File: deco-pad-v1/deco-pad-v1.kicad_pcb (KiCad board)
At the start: 2 copper layers, 86 parts, among them J1 AVR-ISP-6, SW1 EC11, SW2 EC11, SW3 EC11, SW4 SW_Push, U1 ATmega32U4-MU, U2 PRTR5VOU2X, Y1 16MHz

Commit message: [NZ] Still staging
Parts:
- moved H5 48.1 mm to (139.0, 148.0)
- moved J1 41.1 mm to (128.0, 89.5)
- moved SW4 40.5 mm to (118.4, 76.0), turned to 180 degrees
- moved R17 35.3 mm to (124.8, 79.2)
- moved C9 26.6 mm to (114.3, 115.1)
- moved C8 26.4 mm to (129.1, 108.8)
- moved Y1 25.7 mm to (129.1, 112.0)
- moved U1 25.6 mm to (119.7, 111.3)
- moved C10 25.3 mm to (123.1, 116.7)
- moved C7 24.9 mm to (129.1, 115.2)
- moved C14 24.6 mm to (119.9, 103.5)
- moved C15 24.6 mm to (121.9, 103.5)
- moved C12 24.5 mm to (113.5, 107.1)
- moved C13 24.5 mm to (113.5, 109.1)
- moved C11 24.2 mm to (125.3, 108.3), turned to 90 degrees
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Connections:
- SW1 pad A: E0_PAD_B -> E0_PAD_A
- SW1 pad B: E0_PAD_A -> E0_PAD_B
- SW2 pad A: E1_PAD_B -> E1_PAD_A
- SW2 pad B: E1_PAD_A -> E1_PAD_B
- SW3 pad A: E2_PAD_B -> E2_PAD_A
- SW3 pad B: E2_PAD_A -> E2_PAD_B
- U2 pad 4: VBUS -> Net-(U2-Pad4)
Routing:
- net ROW3: track 0.00 -> 73.0 mm
- net ROW2: track 0.00 -> 73.0 mm
- net ROW1: track 0.00 -> 73.0 mm
- net ROW0: track 0.00 -> 73.0 mm
- net RESET: track 0.00 -> 51.0 mm, vias 0 -> 3
- net D+: track 0.00 -> 44.4 mm
- net D-: track 0.00 -> 44.3 mm
- net GND: track 11.4 -> 39.2 mm
- net SCK: track 0.00 -> 24.4 mm
- net MISO: track 0.00 -> 22.7 mm
- net +5V: track 2.31 -> 23.2 mm
- net MOSI: track 0.00 -> 17.3 mm
- net Net-(R15-Pad2): track 0.00 -> 15.3 mm
- net Net-(R16-Pad1): track 0.00 -> 14.9 mm
- net VBUS: track 8.95 -> 22.2 mm, vias 2 -> 3
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
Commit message: [NZ] PCB ready for review
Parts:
- removed the C3 at (161.0, 41.6)
- removed the C4 at (160.4, 60.8)
- removed the C6 at (134.1, 60.6)
- removed the C9 at (114.3, 115.1)
- removed D20: Schottky, Diode_SMD:D_SOD-123
- removed D21: RED, LED_SMD:LED_0805_2012Metric
- removed R12, R17, R19: 10K, Resistor_SMD:R_0805_2012Metric
- removed R18: 1K, Resistor_SMD:R_0805_2012Metric
- removed the R5 at (194.0, 45.1)
- removed the R6 at (194.0, 57.8)
- removed the R7 at (189.8, 57.8)
- removed the R8 at (189.8, 45.1)
- removed SW3: EC11, Rotary_Encoder:RotaryEncoder_Alps_EC11E-Switch_Vertical_H20mm
- removed SW4: SW_Push, Button_Switch_SMD:SW_SPST_B3S-1000
- C5: value 10n -> 0.1u
- D18: value D_Small -> Schottky
- D19: value D_Small -> RED; footprint Diode_SMD:D_SOD-123 -> LED_SMD:LED_0805_2012Metric
- R10: value 10K -> 1K
- SW2: value EC11 -> SW_Push; footprint Rotary_Encoder:RotaryEncoder_Alps_EC11E-Switch_Vertical_H20mm -> Button_Switch_SMD:SW_SPST_B3S-1000; moved to B.Cu
- moved D19 133.3 mm to (75.7, 47.0), turned to 0 degrees
- moved D18 107.8 mm to (71.5, 45.9), turned to 180 degrees
- moved C1 96.3 mm to (96.5, 70.8)
- moved C2 95.7 mm to (96.5, 53.2)
- moved H5 92.2 mm to (47.5, 159.5)
- moved H3 87.1 mm to (126.5, 159.5)
- moved D1 86.5 mm to (66.5, 91.5)
- moved D10 86.5 mm to (104.5, 110.5)
- moved D11 86.5 mm to (104.5, 129.5)
- moved D12 86.5 mm to (104.5, 148.5)
- moved D13 86.5 mm to (123.5, 91.5)
- moved D14 86.5 mm to (123.5, 110.5)
- moved D15 86.5 mm to (123.5, 129.5)
- moved D16 86.5 mm to (123.5, 148.5)
- moved D2 86.5 mm to (66.5, 110.5)
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- renumbered C14 to C10, C15 to C11, C7 to C3, C8 to C4, C10 to C6, C11 to C7, C12 to C8, C13 to C9, R13 to R5, R14 to R6, R15 to R7, R16 to R8, U2 to U1, U1 to U2
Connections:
- C1 pad 1: E2_PAD_B-F -> E0_PAD_B-F
- C2 pad 1: E2_PAD_A-F -> E0_PAD_A-F
- C5 pad 1: E0_PAD_B-F -> +5V
- D18 pad 1: ROW1 -> +5V
- D19 pad 1: ROW2 -> GND
- F1 pad 1: Net-(D20-Pad2) -> Net-(D18-Pad2)
- R10 pad 2: E1_PAD_A-F -> Net-(D19-Pad2)
- R11 pad 1: +5V -> GND
- R11 pad 2: E0_PAD_B-F -> Net-(R11-Pad2)
- R3 pad 1: E1_PAD_A-F -> +5V
- R3 pad 2: E1_PAD_A -> E0_PAD_B-F
- R4 pad 1: E1_PAD_B-F -> +5V
- R4 pad 2: E1_PAD_B -> E0_PAD_A-F
- R9 pad 2: E1_PAD_B-F -> RESET
- U2 pad 18: ROW0 -> Net-(U2-Pad18)
- U2 pad 19: ROW1 -> Net-(U2-Pad19)
- U2 pad 20: ROW2 -> Net-(U2-Pad20)
- U2 pad 21: ROW3 -> Net-(U2-Pad21)
- U2 pad 25: COL0 -> COL4
- U2 pad 26: COL1 -> COL3
- U2 pad 28: COL3 -> COL1
- U2 pad 29: COL4 -> COL0
- U2 pad 33: Net-(R19-Pad2) -> Net-(R11-Pad2)
- U2 pad 38: E1_PAD_A-F -> ROW0
- U2 pad 39: E1_PAD_B-F -> ROW1
- U2 pad 40: E2_PAD_A-F -> ROW2
- U2 pad 41: E2_PAD_B-F -> ROW3
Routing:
- net ROW3: track 73.0 -> 195.8 mm
- net COL0: track 0.00 -> 116.3 mm, vias 0 -> 1
- net ROW0: track 73.0 -> 185.0 mm
- net COL3: track 0.00 -> 111.4 mm, vias 0 -> 1
- net ROW2: track 73.0 -> 176.6 mm
- net +5V: track 23.2 -> 125.0 mm, vias 0 -> 6
- net COL1: track 0.00 -> 98.1 mm, vias 0 -> 1
- net COL2: track 0.00 -> 91.5 mm, vias 0 -> 1
- net ROW1: track 73.0 -> 157.4 mm
- net COL4: track 0.00 -> 66.4 mm, vias 0 -> 1
- net E0_PAD_A-F: track 0.00 -> 62.0 mm, vias 0 -> 2
- net E0_PAD_B-F: track 0.00 -> 41.0 mm
- net VBUS: track 22.2 -> 59.2 mm, vias 3 -> 5
- net GND: track 39.2 -> 70.6 mm, vias 0 -> 2
- net D+: track 44.4 -> 20.3 mm
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- added copper zone on B.Cu, net GND
- added copper zone on F.Cu, net GND
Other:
- board outline added: 84 x 121 mm
- board text added: "."

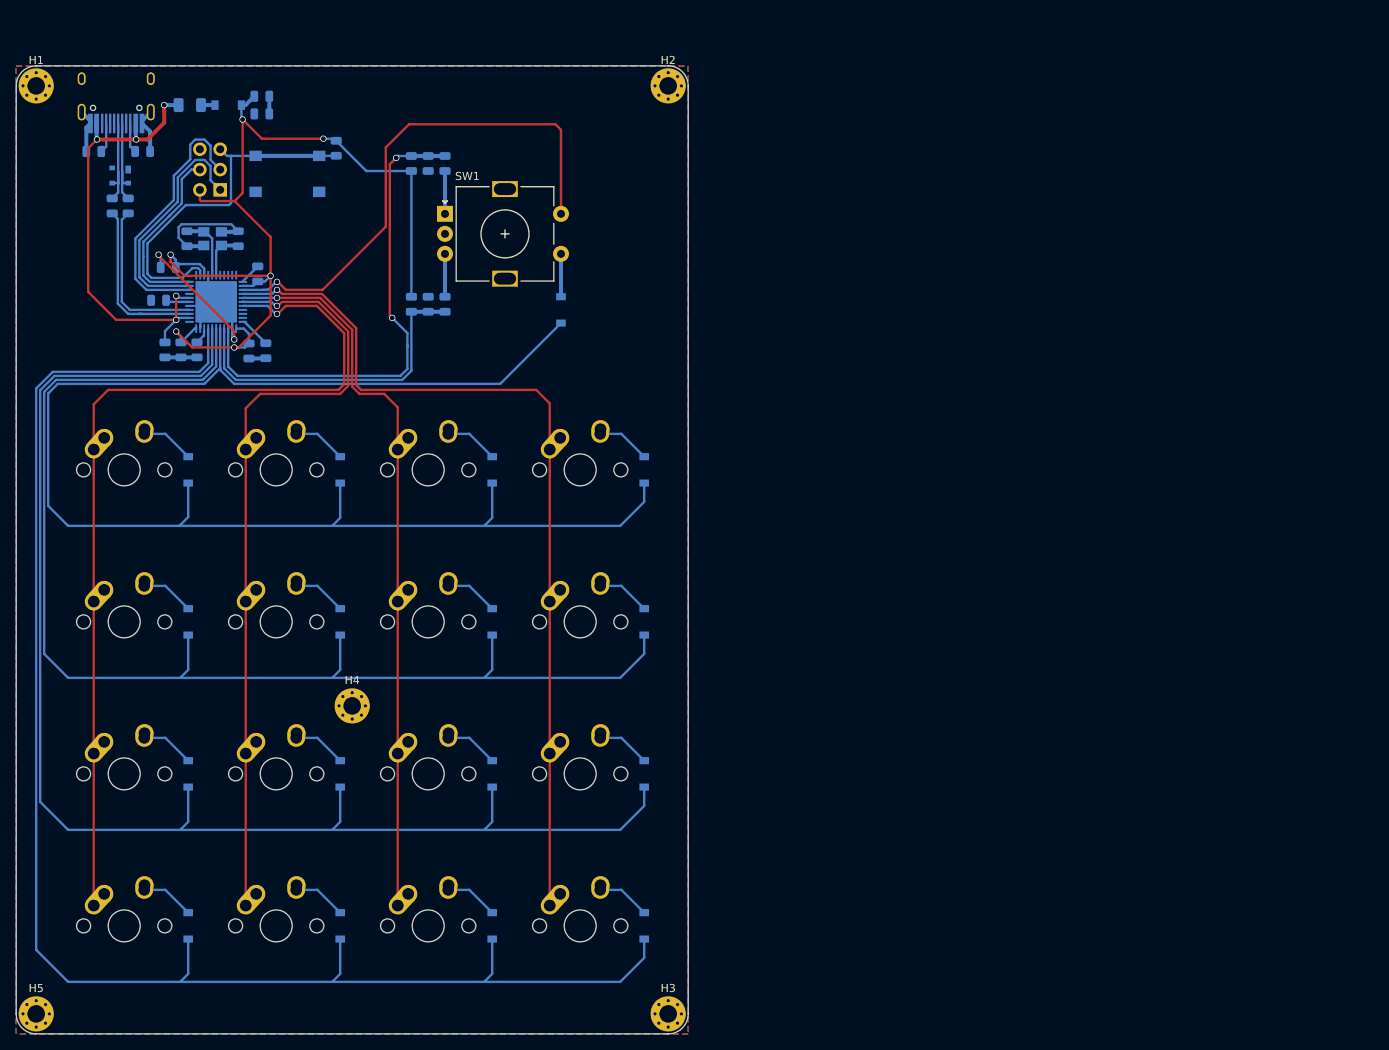
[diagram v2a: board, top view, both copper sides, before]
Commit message: [NZ] Adjusted Rotary Encoder.
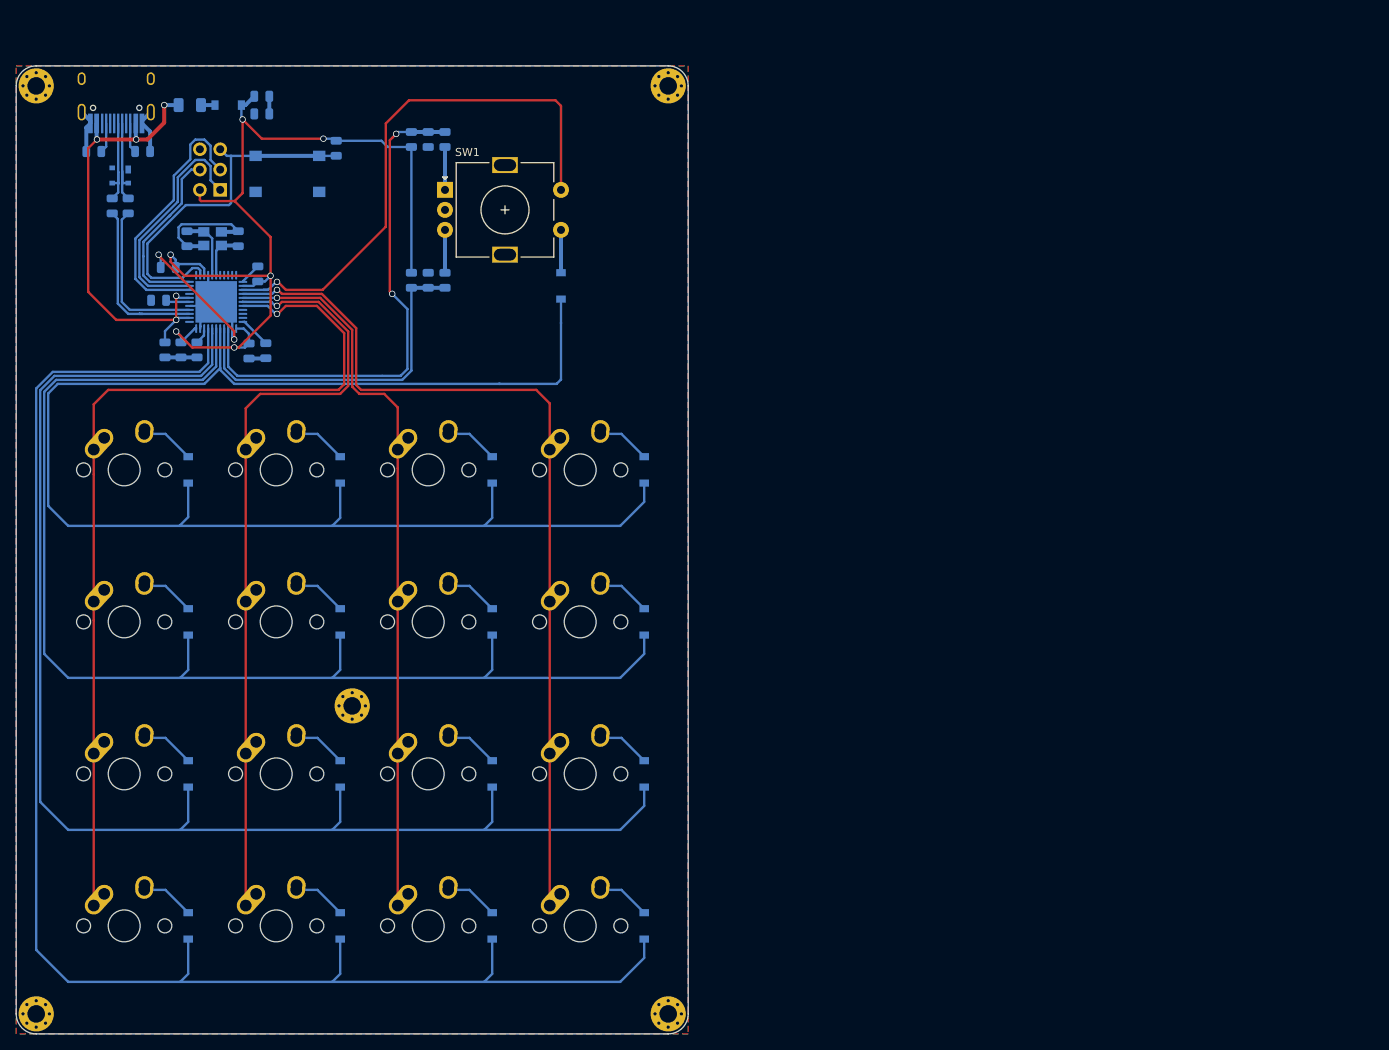
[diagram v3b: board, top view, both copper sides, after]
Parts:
- moved C1 3.00 mm to (96.5, 67.8)
- moved C2 3.00 mm to (96.5, 50.2)
- moved D17 3.00 mm to (113.1, 68.5)
- moved R1 3.00 mm to (98.6, 50.2)
- moved R2 3.00 mm to (98.6, 67.8)
- moved R3 3.00 mm to (94.4, 67.8)
- moved R4 3.00 mm to (94.4, 50.2)
- moved SW1 3.00 mm to (98.6, 56.5)
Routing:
- net ROW0: track 185.0 -> 192.2 mm
- net E0_PAD_B-F: track 41.0 -> 44.0 mm
- net COL4: track 66.4 -> 69.4 mm
- net E0_PAD_A-F: track 62.0 -> 64.8 mm
- net +5V: track 125.0 -> 123.8 mm

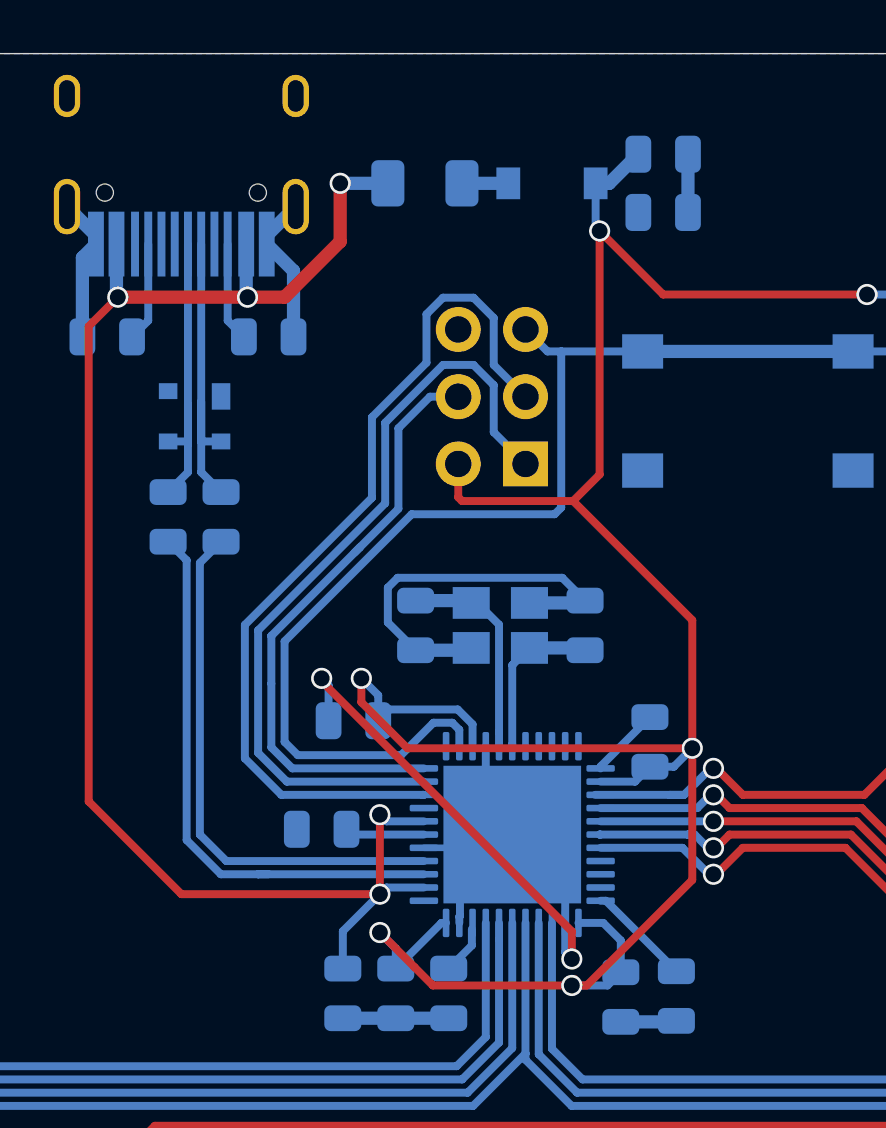
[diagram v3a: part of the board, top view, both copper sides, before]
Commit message: [NZ] Removed ESD while research a backup. Remove schottky since not needed and would drop the voltage too much. Some cleanup. Will add silk art and curved tracks next.
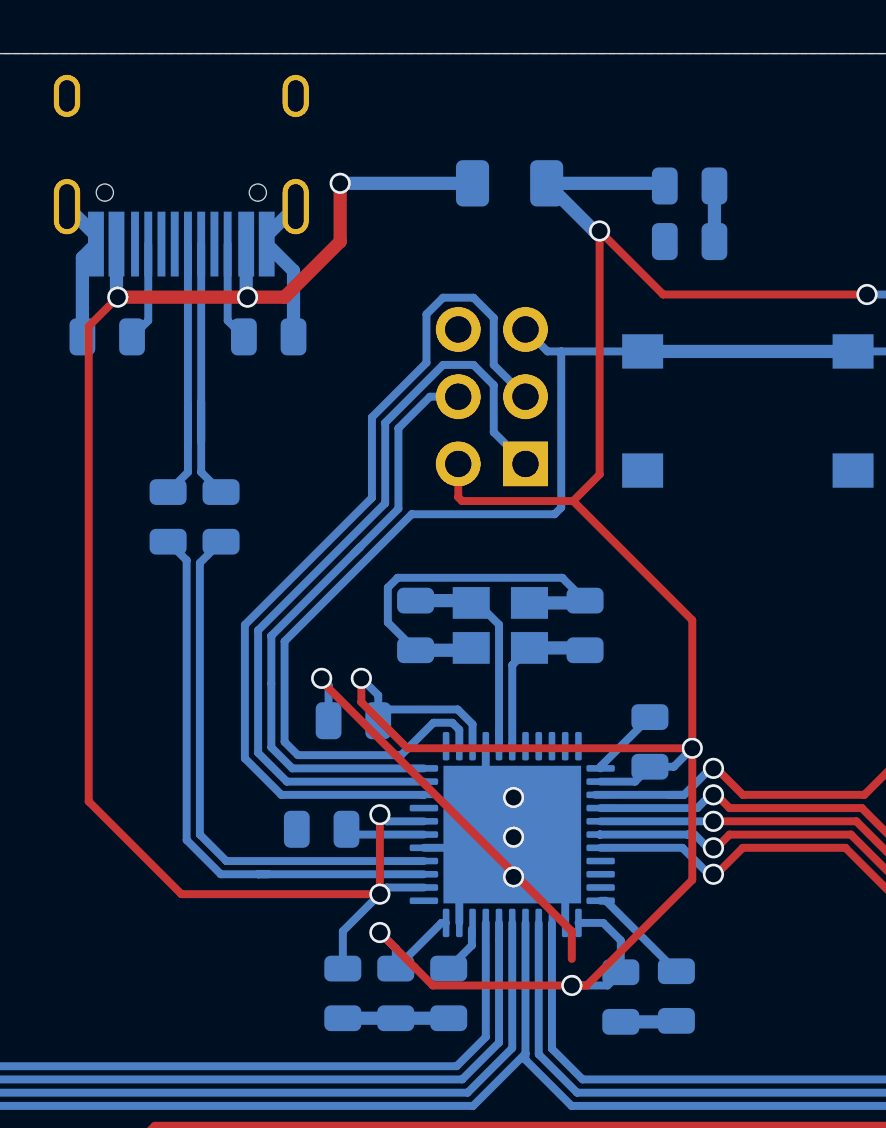
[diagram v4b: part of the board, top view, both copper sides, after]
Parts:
- removed D19: RED, LED_SMD:LED_0805_2012Metric
- removed the R10 at (75.7, 44.8)
- removed U2: ATmega32U4-MU, Package_DFN_QFN:QFN-44-1EP_7x7mm_P0.5mm_EP5.2x5.2mm
- added R5: 1K, Resistor_SMD:R_0805_2012Metric, B.Cu at (76.7, 46.0)
- C1, C2: value 10n -> 0.01u
- C9: value 100n -> 0.1u
- D18: value Schottky -> RED; footprint Diode_SMD:D_SOD-123 -> LED_SMD:LED_0805_2012Metric
- U1: value PRTR5VOU2X -> ATmega32U4-MU; footprint Nexperia:SOT143B -> Package_DFN_QFN:QFN-44-1EP_7x7mm_P0.5mm_EP5.2x5.2mm
- moved U1 19.8 mm to (70.0, 70.5), turned to 0 degrees
- moved D18 5.65 mm to (76.7, 48.1), turned to 0 degrees
- moved F1 3.20 mm to (69.9, 45.9)
- renumbered R5 to R1, R9 to R10, R6 to R2, R7 to R3, R8 to R4, R1 to R6, R2 to R7, R3 to R8, R4 to R9
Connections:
- D18 pad 1: +5V -> GND
- F1 pad 1: Net-(D18-Pad2) -> +5V
- R3 pad 2: Net-(R7-Pad2) -> Net-(R3-Pad2)
- R4 pad 1: Net-(R8-Pad1) -> Net-(R4-Pad1)
- U1 pad 1: GND -> Net-(U1-Pad1)
- U1 pad 2: Net-(R8-Pad1) -> VBUS
- U1 pad 3: Net-(R7-Pad2) -> D-
- U1 pad 4: Net-(U1-Pad4) -> D+
- USB1 pad 5: Net-(R7-Pad2) -> Net-(R3-Pad2)
- USB1 pad 6: Net-(R8-Pad1) -> Net-(R4-Pad1)
- USB1 pad 7: Net-(R7-Pad2) -> Net-(R3-Pad2)
- USB1 pad 8: Net-(R8-Pad1) -> Net-(R4-Pad1)
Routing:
- net Net-(R7-Pad2): track 12.4 -> 0.00 mm
- net Net-(R8-Pad1): track 11.9 -> 0.00 mm
- net Net-(R3-Pad2): track 0.00 -> 11.6 mm
- net Net-(R4-Pad1): track 0.00 -> 11.2 mm
- net GND: track 70.6 -> 67.1 mm, vias 2 -> 4
- net +5V: track 123.8 -> 127.3 mm
- net VBUS: track 59.2 -> 62.4 mm
- net Net-(D19-Pad2): track 2.20 -> 0.00 mm
